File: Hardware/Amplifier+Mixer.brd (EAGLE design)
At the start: 140 x 140 mm, 193 parts, among them IC1 7812, IC2 7805, IC3 7912, IC4 OPA134PA, IC5 OPA134PA, IC6 MEGA8-AI, IC8 LM358D, IC9 LM358D, J1 6MM, J10 JST-XH2, J2 6MM, J3 6MM, J4 6MM, J5 TERMINAL-BLOCK-2PLUG-IN, J6 TERMINAL-BLOCK-2PLUG-IN, J7 ENCODER, J8 DISPLAY, J9 USB, K1 12V 8A, K2 12V 8A, T1 BC817, T2 BC817, T3 BC817, U1 LM1117-3.3, U2 10k, U3 10k, U4 10k, U5 10k, U6 TDA7498L, U7 10k, U8 10k, U9 MCP9700SMD, X1 RCA-4-CHANNEL, X2 JST-XH2, X3 ICSP, X4 JST-XH2

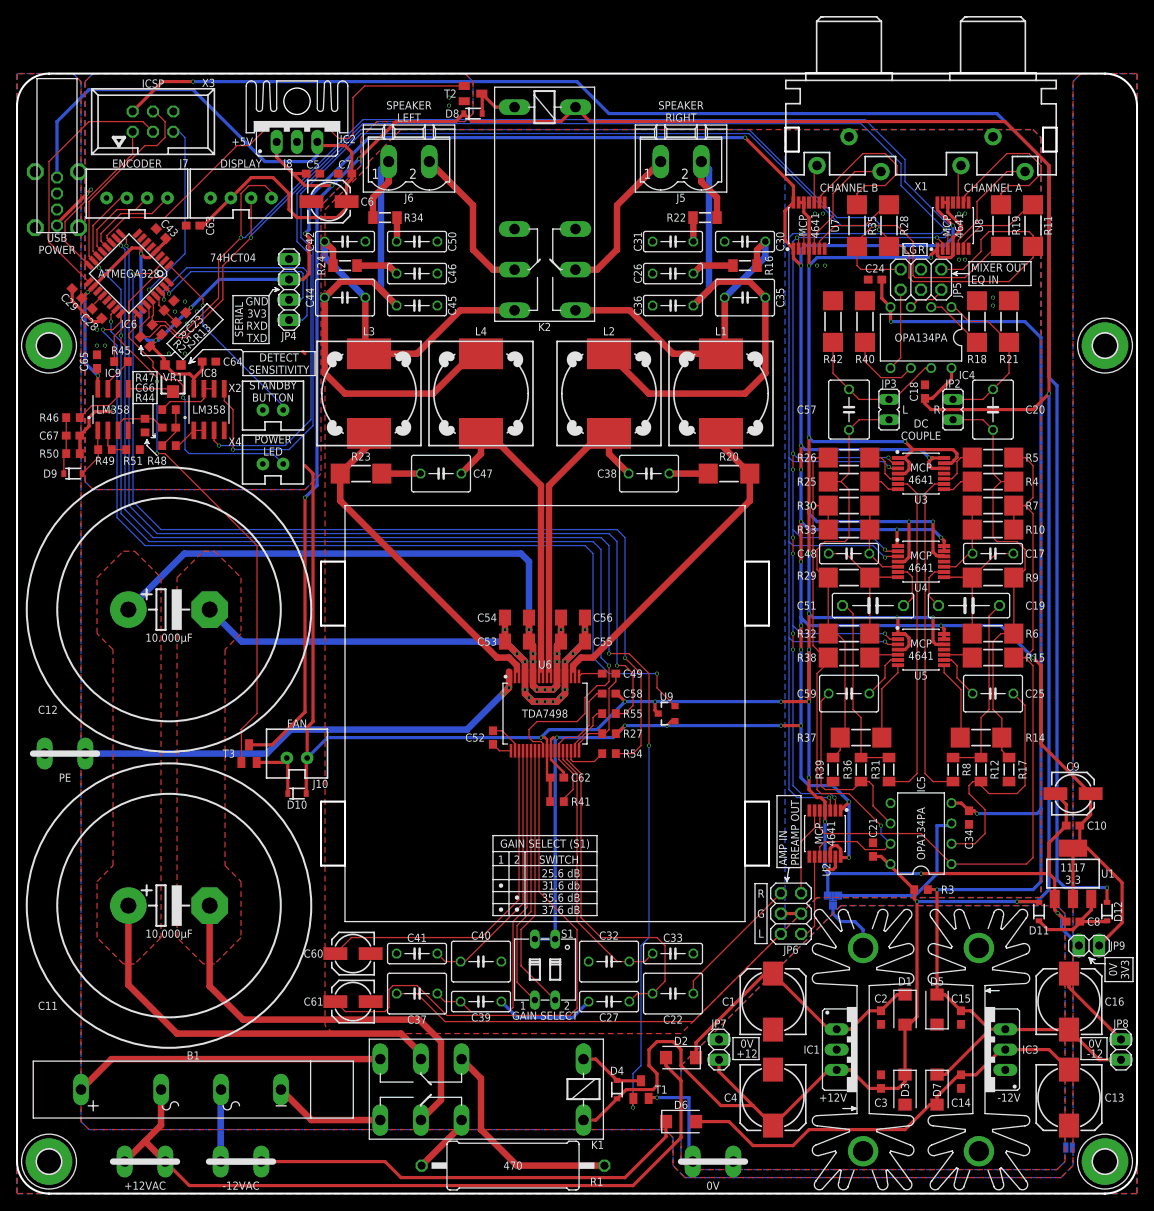
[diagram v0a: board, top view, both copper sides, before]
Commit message: removed gain selection dip switch and wired gain pins to µC
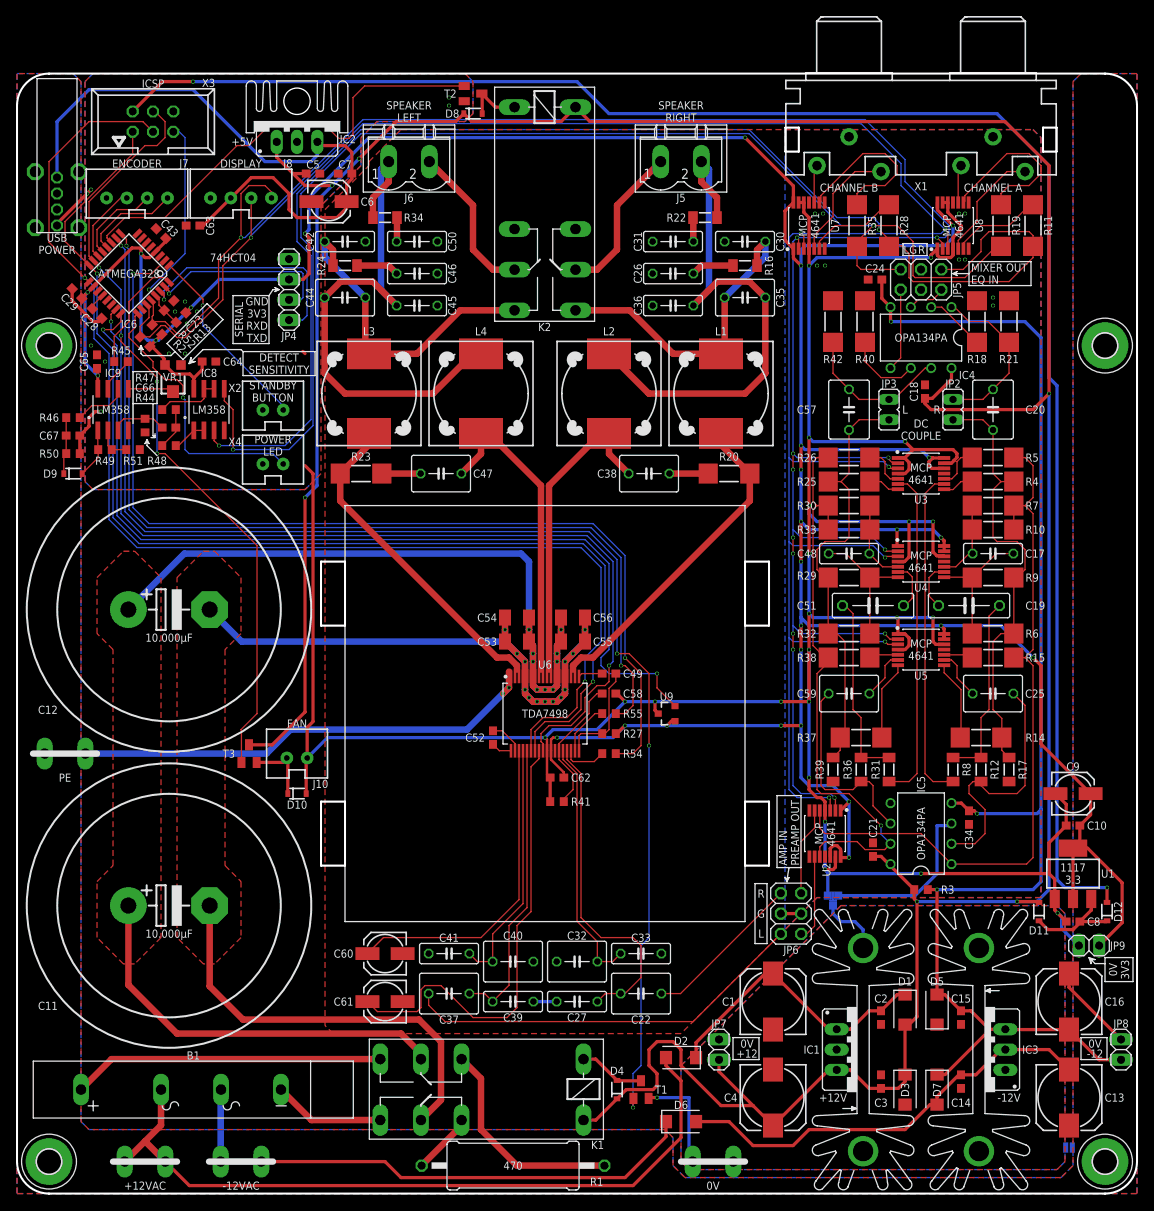
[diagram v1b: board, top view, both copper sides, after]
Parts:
- removed S1: GAIN SELECT, switch-dil:DIP02YL
- moved C22 4.00 mm to (78.0, 25.0)
- moved C27 4.00 mm to (70.0, 24.0)
- moved C32 4.00 mm to (70.0, 29.0)
- moved C33 4.00 mm to (78.0, 30.0)
- moved C37 4.00 mm to (54.0, 25.0)
- moved C39 4.00 mm to (62.0, 24.0)
- moved C40 4.00 mm to (62.0, 29.0)
- moved C41 4.00 mm to (54.0, 30.0)
- moved C60 4.00 mm to (46.0, 30.0)
- moved C61 4.00 mm to (46.0, 24.0)
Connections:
- removed net N$79: IC6.16, X3.1
- removed net N$80: IC6.17, X3.3
- net +3V3: no longer S1.1, S1.2
- net GAIN0: now also IC6.16, X3.1; no longer S1.4
- net GAIN1: now also IC6.17, X3.3; no longer S1.3
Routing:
- net GAIN1: track 32.8 -> 156.5 mm, vias 0 -> 2
- net GAIN0: track 33.7 -> 146.8 mm, vias 0 -> 2
- net N$80: track 32.7 -> 0.00 mm
- net +3V3: track 474.4 -> 446.6 mm
- net N$79: track 21.4 -> 0.00 mm
- net N$66: track 69.5 -> 57.3 mm
- net AGND: track 36.5 -> 26.9 mm
- net INPB: track 43.5 -> 36.5 mm
- net N$65: track 44.4 -> 40.4 mm
- net N$84: track 54.0 -> 50.9 mm
- net N$81: track 17.1 -> 20.1 mm
- net AMP_DIAG: track 122.7 -> 120.0 mm
- net INNA: track 34.0 -> 31.5 mm
- net INPA: track 43.5 -> 41.2 mm
- net DGND: track 401.3 -> 399.2 mm, vias 36 -> 35
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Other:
- board text removed: "1"
- board text removed: "2"
- board text removed: "25.6 dB 31.6 db 35.6 dB 37.6 dB"
- board text removed: "GAIN SELECT"
- board text removed: "GAIN SELECT (S1)"
- board text removed: "SWITCH"

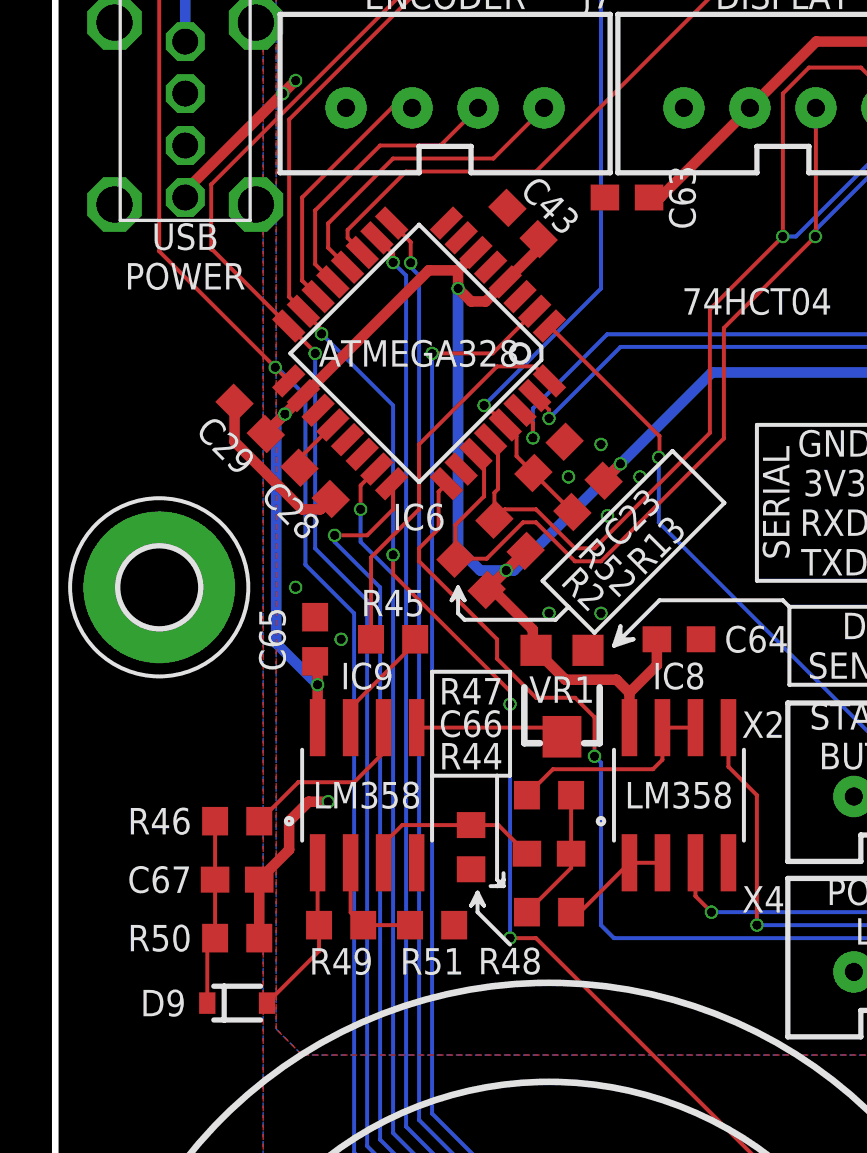
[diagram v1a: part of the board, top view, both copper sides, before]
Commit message: added indicator LED to audio detection circuit
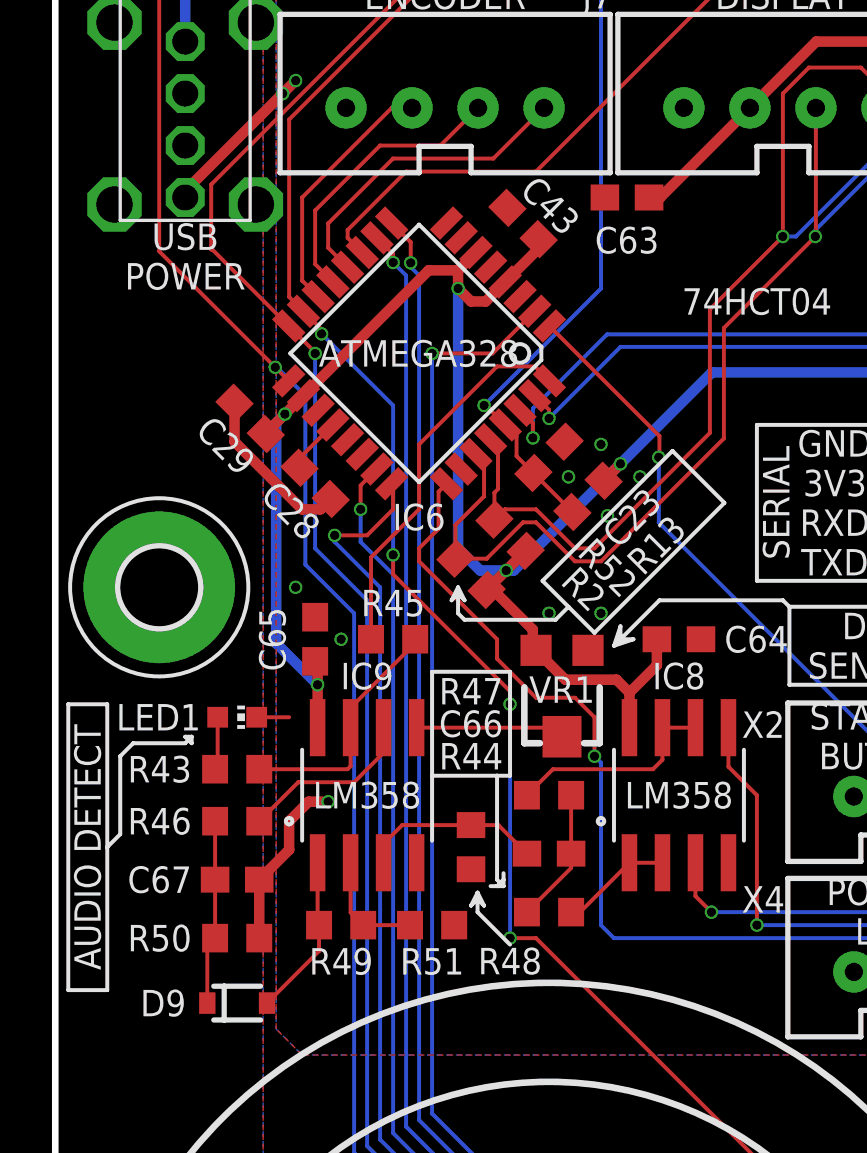
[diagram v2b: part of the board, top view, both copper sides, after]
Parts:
- added LED1: (no value), led:CHIP-LED0603
- added R43: 1k, rcl:R0603
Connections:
- new net N$37: LED1.A, R43.2
- net +3V3: now also U2.11, U3.11, U4.11, U5.11, U7.11, U8.11
- net DGND: now also LED1.C
- net N$36: now also R43.1
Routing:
- net N$36: track 4.43 -> 9.48 mm
- net N$37: track 0.00 -> 2.04 mm
- net DGND: track 399.2 -> 400.5 mm
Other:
- board text added: "AUDIO DETECT"
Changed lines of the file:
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@@
 <text x="32" y="92.25" size="1.016" layer="21" ratio="14" align="bottom-center">POWER
 LED</text>
+<text x="1.75" y="96" size="1.016" layer="25" ratio="14" rot="R90" align="bottom-center">AUDIO DETECT</text>
+<wire x1="2.5" y1="96.5" x2="2.5" y2="99.5" width="0.1524" layer="25"/>
+<wire x1="2.5" y1="99.5" x2="3" y2="100" width="0.1524" layer="25"/>
+<wire x1="3" y1="100" x2="5" y2="100" width="0.1524" layer="25"/>
+<wire x1="5" y1="100" x2="5.25" y2="100.25" width="0.1524" layer="25"/>
+<wire x1="5.25" y1="100.25" x2="5" y2="100.25" width="0.1524" layer="25"/>
+<wire x1="5" y1="100.25" x2="5.25" y2="100" width="0.1524" layer="25"/>
+<wire x1="5.25" y1="100" x2="5.25" y2="100.25" width="0.1524" layer="25"/>
+<wire x1="2" y1="90.5" x2="0.5" y2="90.5" width="0.1524" layer="25"/>
+<wire x1="0.5" y1="90.5" x2="0.5" y2="101.5" width="0.1524" layer="25"/>
+<wire x1="0.5" y1="101.5" x2="2" y2="101.5" width="0.1524" layer="25"/>
+<wire x1="2" y1="101.5" x2="2" y2="96" width="0.1524" layer="25"/>
+<wire x1="2" y1="96" x2="2" y2="90.5" width="0.1524" layer="25"/>
+<wire x1="2" y1="96" x2="2.5" y2="96.5" width="0.1524" layer="25"/>
 </plain>
 <attributes>
@@
 <attribute name="CONRAD" value="457901 - 62" x="22" y="121" size="1.778" layer="27" display="off"/>
 <attribute name="MOUSER" value="710-885012206071" x="22" y="121" size="1.778" layer="27" display="off"/>
-<attribute name="NAME" x="23.6254" y="121" size="1.016" layer="25" ratio="14" rot="R270" align="bottom-center"/>
+<attribute name="NAME" x="22" y="119.8646" size="1.016" layer="25" ratio="14" align="top-center"/>
 <attribute name="SPICEPREFIX" value="C" x="52.48" y="-37.75" size="1.778" layer="27" display="off"/>
 <attribute name="STOCK" value="24" x="22" y="121" size="1.778" layer="27" display="off"/>
@@
 <attribute name="VALUE" x="33" y="95.75" size="0.4064" layer="27"/>
 </element>
+<element name="LED1" library="led" library_urn="urn:adsk.eagle:library:259" package="CHIP-LED0603" package3d_urn="urn:adsk.eagle:package:15819/3" value="" x="7" y="101" smashed="yes" rot="R270">
+<attribute name="NAME" x="5.6" y="101" size="1.016" layer="25" ratio="14" align="center-right"/>
+<attribute name="VALUE" x="6.365" y="99.095" size="1.27" layer="27"/>
+</element>
+<element name="R43" library="rcl" library_urn="urn:adsk.eagle:library:334" package="R0603" package3d_urn="urn:adsk.eagle:package:23555/3" value="1k" x="7" y="99" smashed="yes" rot="R180">
+<attribute name="CONRAD" value="1585255 - 62" x="7" y="99" size="1.016" layer="27" ratio="14" rot="R180" display="off"/>
+<attribute name="MOUSER" value="603-RC0603FR-071KL" x="7" y="99" size="1.016" layer="27" ratio="14" rot="R180" display="off"/>
+<attribute name="NAME" x="5.2516" y="99" size="1.016" layer="25" ratio="14" align="center-right"/>
+<attribute name="SPICEPREFIX" value="R" x="7" y="99" size="1.016" layer="27" ratio="14" rot="R180" display="off"/>
+<attribute name="STOCK" value="3" x="7" y="99" size="1.016" layer="27" ratio="14" rot="R180" display="off"/>
+<attribute name="VALUE" x="7.635" y="100.905" size="1.27" layer="27" rot="R180"/>
+</element>
 </elements>
 <signals>
@@
 <wire x1="81.25" y1="58.5" x2="81.8" y2="59.05" width="0.4064" layer="1"/>
 <wire x1="81.8" y1="59.05" x2="82.25" y2="59.05" width="0.4064" layer="1"/>
+<contactref element="U4" pad="11"/>
+<contactref element="U5" pad="11"/>
+<contactref element="U3" pad="11"/>
+<contactref element="U2" pad="11"/>
+<contactref element="U7" pad="11"/>
+<contactref element="U8" pad="11"/>
+<wire x1="115.05" y1="123.8866" x2="117" y2="123.8866" width="0" layer="19" extent="1-1"/>
+<wire x1="115.8866" y1="90" x2="115.8866" y2="90.65" width="0" layer="19" extent="1-1"/>
+<wire x1="101" y1="42.1134" x2="101.65" y2="42.1134" width="0" layer="19" extent="1-1"/>
+<wire x1="115.8866" y1="79" x2="115.8866" y2="80.3" width="0" layer="19" extent="1-1"/>
+<wire x1="115.8866" y1="68" x2="115.8866" y2="69.3" width="0" layer="19" extent="1-1"/>
+<wire x1="99" y1="123.8866" x2="97.05" y2="123.8866" width="0" layer="19" extent="1-1"/>
 </signal>
 <signal name="AUDIO_DETECT">
@@
 <wire x1="13.85" y1="103.85" x2="11.365" y2="101.365" width="0.1524" layer="1"/>
 <wire x1="11.365" y1="101.365" x2="11.365" y2="100.6" width="0.1524" layer="1"/>
+<contactref element="R43" pad="1"/>
+<wire x1="11.365" y1="100.6" x2="11.365" y2="99.115" width="0.1524" layer="1"/>
+<wire x1="11.365" y1="99.115" x2="11.25" y2="99" width="0.1524" layer="1"/>
+<wire x1="11.25" y1="99" x2="7.85" y2="99" width="0.1524" layer="1"/>
 </signal>
 <signal name="N$38">
@@
 <via x="11" y="104" extent="1-16" drill="0.35" shape="octagon"/>
 <via x="9.25" y="106" extent="1-16" drill="0.35" shape="octagon"/>
+<contactref element="LED1" pad="C"/>
+<wire x1="7.75" y1="101" x2="9" y2="101" width="0.1524" layer="1"/>
 </signal>
 <signal name="AGND">
@@
 <wire x1="31.97" y1="92.5" x2="21.5" y2="92.5" width="0.1524" layer="16"/>
 </signal>
+<signal name="N$37">
+<contactref element="R43" pad="2"/>
+<contactref element="LED1" pad="A"/>
+<wire x1="6.15" y1="99" x2="6.25" y2="99.1" width="0.1524" layer="1"/>
+<wire x1="6.25" y1="99.1" x2="6.25" y2="101" width="0.1524" layer="1"/>
+</signal>
 </signals>
